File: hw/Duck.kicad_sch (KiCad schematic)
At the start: 36 parts, among them J1 Conn_01x06, J2 Conn_01x06, J3 USB_C_Receptacle_USB2.0_14P, Q1 MMBT3904, Q2 MMBT3904, U1 ESP32-S3-PICO-1, U2 SPX3819M5-L-3-3, U3 INMP441, U4 MAX17048G+T10, U5 CH343P

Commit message: hw: Complete revision
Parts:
- removed JP1: SolderJumper_2_Bridged, Jumper:SolderJumper-2_P1.3mm_Bridged_RoundedPad1.0x1.5mm, symbol Jumper:SolderJumper_2_Bridged
- added C11: 1u, Capacitor_SMD:C_0402_1005Metric, symbol Device:C
- added C12: 10n, Capacitor_SMD:C_0402_1005Metric, symbol Device:C
- added C13: 4.7u, Capacitor_SMD:C_0402_1005Metric, symbol Device:C
- added U6: SPX3819M5-L-3-3, Package_TO_SOT_SMD:SOT-23-5, symbol Regulator_Linear:SPX3819M5-L-3-3
- J1: footprint Duck_footprints:TestPoints_1x06_P2.0 -> Duck_footprints:TestPoints_FFC_1x06_P0.5
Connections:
- net +3V3: now also J1.1 (Pin_1), J2.1 (Pin_1), C13.1, U6.5 (OUT)
- net +BATT: no longer J1.1 (Pin_1), J2.1 (Pin_1)
- net BOOT0: now also J1.4 (Pin_4), J2.4 (Pin_4); no longer J1.6 (Pin_6), J2.6 (Pin_6)
- net ESP_EN: now also J1.2 (Pin_2), J2.2 (Pin_2), C11.1; no longer J1.5 (Pin_5), J2.5 (Pin_5)
- net GND: now also J1.3 (Pin_3), J2.3 (Pin_3), C11.2, C12.2, C13.2, U6.2 (GND); no longer J1.2 (Pin_2), J2.2 (Pin_2)
- net U0RXD: now also J1.5 (Pin_5), J2.5 (Pin_5), U1.14 (GPIO9); no longer J1.4 (Pin_4), J2.4 (Pin_4)
- net U0TXD: now also J1.6 (Pin_6), J2.6 (Pin_6), U1.22 (GPIO16/XTAL_32K_N); no longer J1.3 (Pin_3), J2.3 (Pin_3)
- net VBUS: now also U6.1 (IN), U6.3 (EN)
- new net: C12.1, U6.4 (BP)
- no-connect marks 35 -> 33
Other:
- moved on the sheet: Q1, Q2, R10, R9

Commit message: hw: Schematic page layout
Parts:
- J1: value Conn_01x06 -> FFC P0.5
- J2: value Conn_01x06 -> Pin P2.54
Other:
- note added: "Application"
- note added: "Debugger"
- moved on the sheet: AE1, BT1, C1, C10, C11, C12, C13, C2, C3, C4, C5, C6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

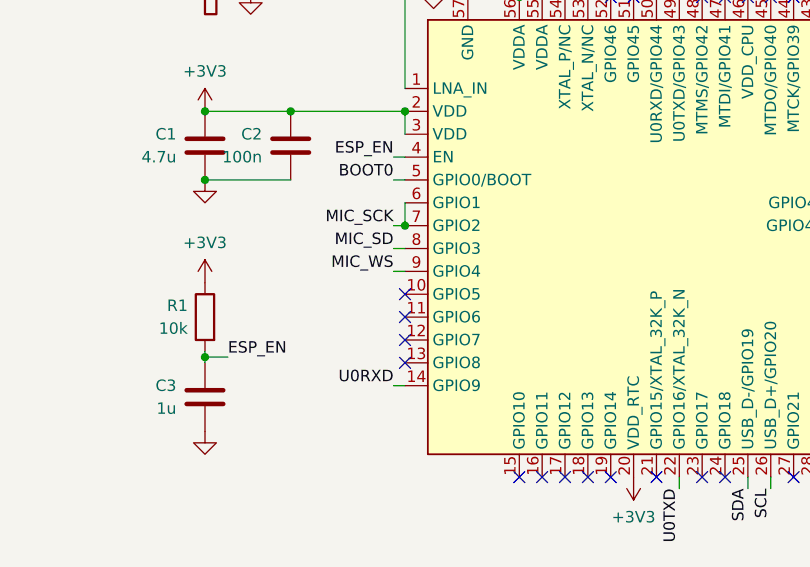
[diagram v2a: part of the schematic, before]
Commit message: hw: Revise schematic and update PCB; resubmit (Rev. 2)
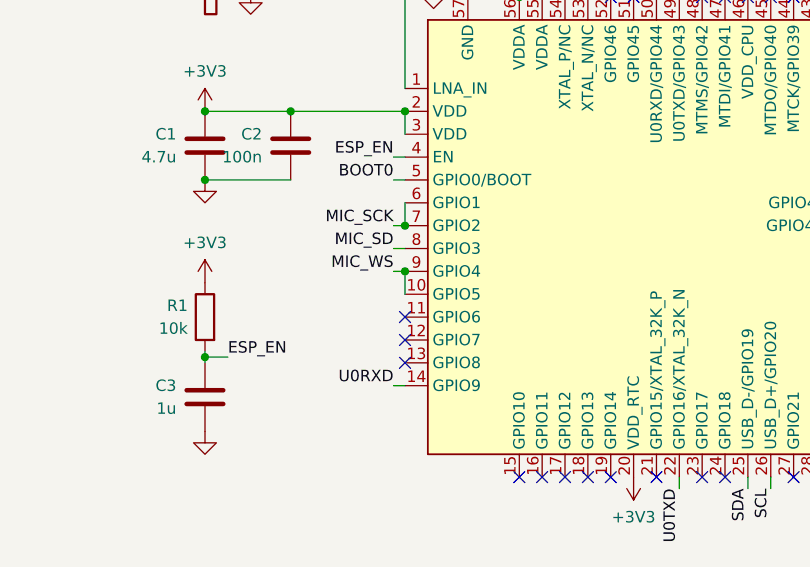
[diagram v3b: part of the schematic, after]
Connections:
- net MIC_WS: now also U1.10 (GPIO5)
- no-connect marks 33 -> 32
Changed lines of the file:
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@@
   (junction (at 88.9 110.49) (diameter 0) (color 0 0 0 0)
+  )
+  (junction (at 186.69 60.325) (diameter 0) (color 0 0 0 0)
   )
   (junction (at 42.545 136.525) (diameter 0) (color 0 0 0 0)
@@
   (no_connect (at 265.43 113.665))
   (no_connect (at 227.33 29.845))
-  (no_connect (at 186.69 62.865))
   (no_connect (at 222.25 29.845))
   (no_connect (at 95.885 63.5))
@@
     (stroke (width 0) (type default))
   )
+  (wire (pts (xy 186.69 60.325) (xy 186.69 62.865))
+    (stroke (width 0) (type default))
+  )

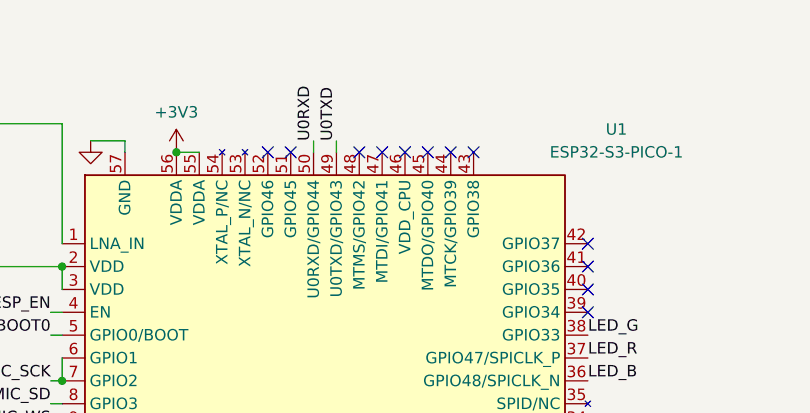
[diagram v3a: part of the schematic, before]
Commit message: hw: Fix missing power line (/_<); resubmit (Rev. 2)
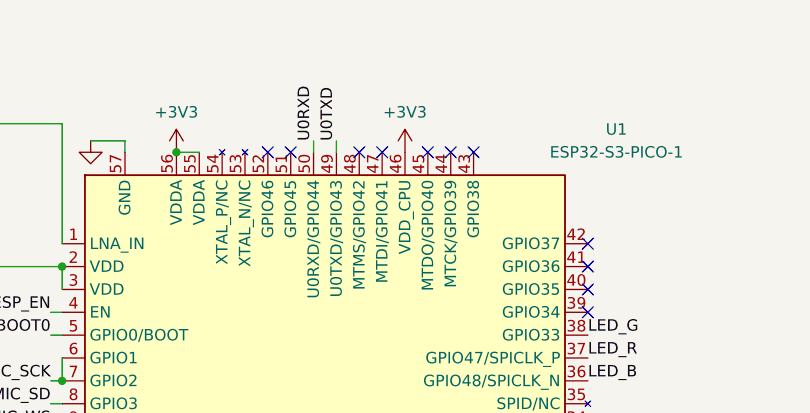
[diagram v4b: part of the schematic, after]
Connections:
- net +3V3: now also U1.46 (VDD_CPU)
- no-connect marks 32 -> 31
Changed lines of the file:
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@@
   (no_connect (at 83.82 76.835))
   (no_connect (at 234.95 108.585))
-  (no_connect (at 224.79 29.845))
   (no_connect (at 232.41 29.845))
   (no_connect (at 201.93 83.185))
@@
         )
       )
+    )
+  )
+  (symbol (lib_id "power:+3V3") (at 224.79 29.845 0) (unit 1)
+    (in_bom yes) (on_board yes) (dnp no) (fields_autoplaced)
+    (property "Reference" "#PWR043" (at 224.79 33.655 0)
+      (effects (font (size 1.27 1.27)) hide)
+    )
+    (property "Value" "+3V3" (at 224.79 25.4 0)
+      (effects (font (size 1.27 1.27)))
+    )
+    (property "Footprint" "" (at 224.79 29.845 0)
+      (effects (font (size 1.27 1.27)) hide)
+    )
+    (property "Datasheet" "" (at 224.79 29.845 0)
+      (effects (font (size 1.27 1.27)) hide)
+    )
+    (pin "1")
+    (instances
+      (project "Duck"
+        (path "/23349607-acbb-4aa4-80bb-d6050790beec"
+          (reference "#PWR043") (unit 1)
+        )
+      )
